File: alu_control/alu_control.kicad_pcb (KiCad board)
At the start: 2 copper layers, 43.8 x 62.2 mm, 52 parts

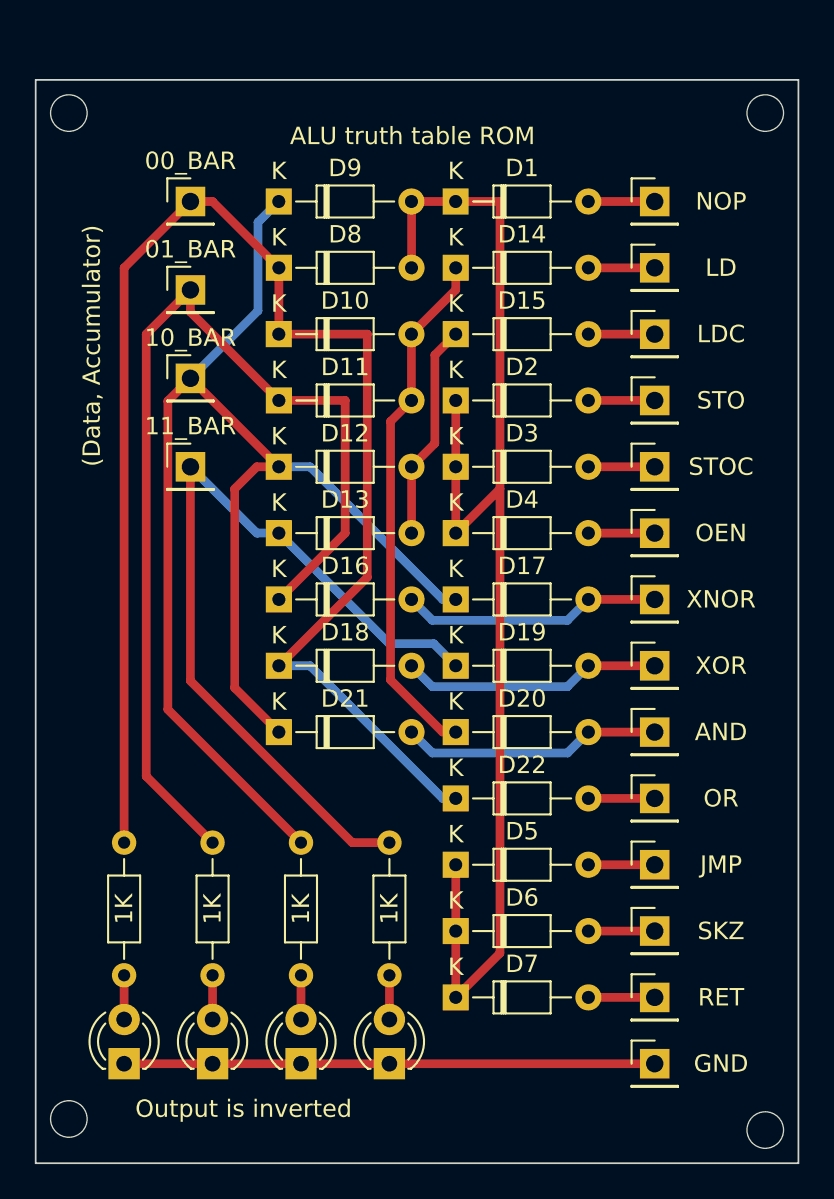
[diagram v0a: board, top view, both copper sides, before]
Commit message: Fix missing instruction on rom
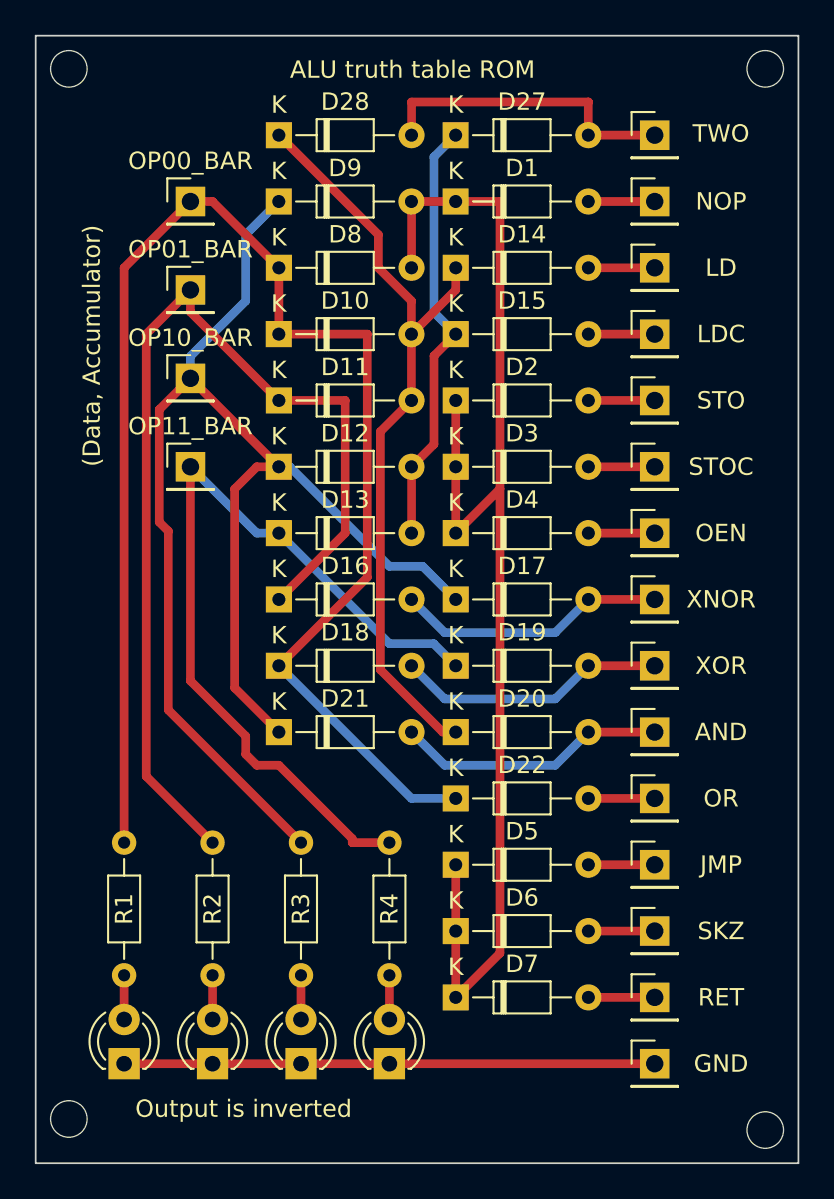
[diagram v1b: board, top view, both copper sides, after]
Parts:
- added D27: D, Diode_THT:D_DO-34_SOD68_P7.62mm_Horizontal, F.Cu at (45.1, 24.8)
- added D28: D, Diode_THT:D_DO-34_SOD68_P7.62mm_Horizontal, F.Cu at (34.9, 24.8)
- added TWO: Conn_01x01_Pin, Connector_PinHeader_2.54mm:PinHeader_1x01_P2.54mm_Vertical, F.Cu at (56.5, 24.8)
- R1: renamed from 1K; value 2K -> 1K
- moved REF** 2.54 mm to (22.9, 21.0)
- moved REF** 2.54 mm to (62.9, 21.0)
- renumbered 00_BAR to OP00_BAR, 01_BAR to OP01_BAR, 10_BAR to OP10_BAR, 11_BAR to OP11_BAR, 1K to R2, 1K to R3, 1K to R4
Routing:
- net Net-(D27-A): track 0.00 -> 17.8 mm
- net Net-(D10-A): track 30.2 -> 45.3 mm
- net Net-(D12-A): track 12.5 -> 25.0 mm
- net Net-(D13-K): track 48.0 -> 48.7 mm
- net Net-(D16-A): track 15.0 -> 15.5 mm
- net Net-(D18-A): track 15.0 -> 15.5 mm
- net Net-(AND1-Pin_1): track 15.0 -> 15.5 mm
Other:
- board size 43.8 x 62.2 mm -> 43.8 x 64.8 mm
